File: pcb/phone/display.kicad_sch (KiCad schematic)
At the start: 6 parts

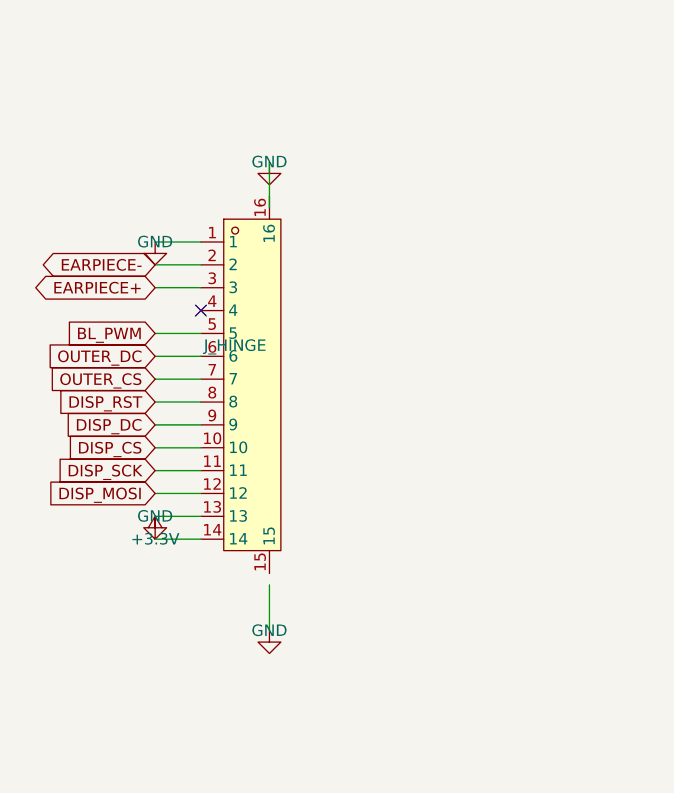
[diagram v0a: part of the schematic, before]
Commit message: Fix display sheet: J_HINGE mounting tab pins 15/16 GND connection
The J_HINGE connector (0.5K-HX-14PWB FPC) has 16 pins in its lib_symbol
definition: 14 signal pins + 2 mounting tabs (pins 15/16). The mounting
tabs need to be connected to GND.

Two issues fixed:
1. Removed phantom pin 15/16 definitions from the symbol instance that
   didn't match the 14-pin lib_symbol (but the lib_symbol itself does
   define 16 pins including the mounting tabs)
2. The GND wires for pins 15/16 were 1.27mm short of the actual pin
   connection points. Extended wire endpoints from (133.81, 109.68) to
   (133.81, 108.41) and from (133.81, 151.59) to (133.81, 150.32) to
   reach the actual pin positions.

Result: Display sheet is now ERC-clean (0 errors, 0 warnings).
Total ERC violations dropped from 287 to 283.

Generated with [Devin](https://devin.ai)

Co-Authored-By: Devin <158243242+devin-ai-integration[bot]@users.noreply.github.com>
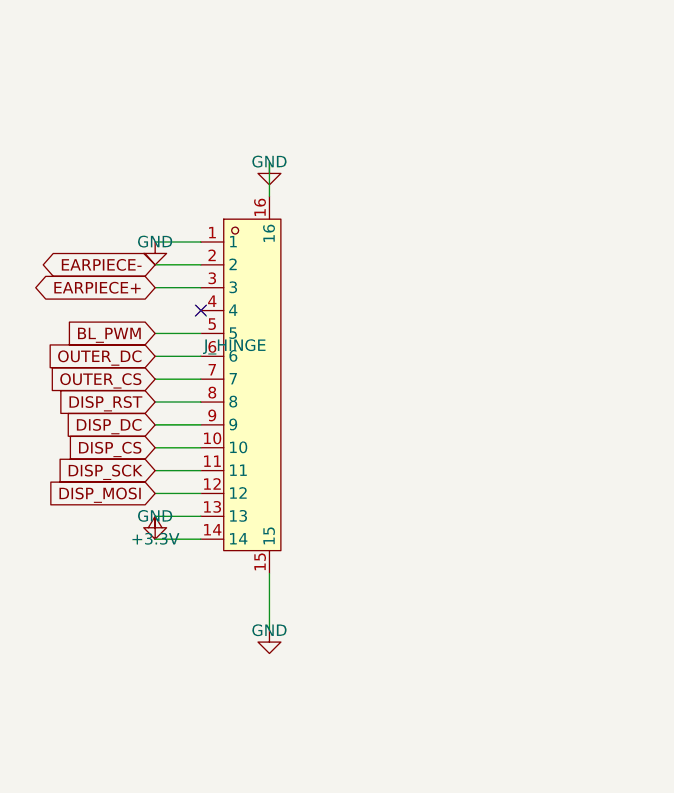
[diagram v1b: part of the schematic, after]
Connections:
- net GND: now also J_HINGE.15, J_HINGE.16
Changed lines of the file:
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@@
 		(wire
 			(pts
-				(xy 133.81 109.68) (xy 133.81 104.60)
-			)
-			(stroke
-				(width 0)
-				(type default)
-			)
-		)
-		(wire
-			(pts
-				(xy 133.81 151.59) (xy 133.81 156.67)
+				(xy 133.81 108.41) (xy 133.81 104.60)
+			)
+			(stroke
+				(width 0)
+				(type default)
+			)
+		)
+		(wire
+			(pts
+				(xy 133.81 150.32) (xy 133.81 156.67)
 			)
 			(stroke
@@
 			(pin "13")
 			(pin "14")
-			(pin "15")
-			(pin "16")
 			(instances (project "phone" (path "/451c3b43-1616-42cb-bf96-d436f4db82c2/d7f57b90-9db7-4266-b1f1-7949b1054009" (reference "J_HINGE") (unit 1))))
 		)

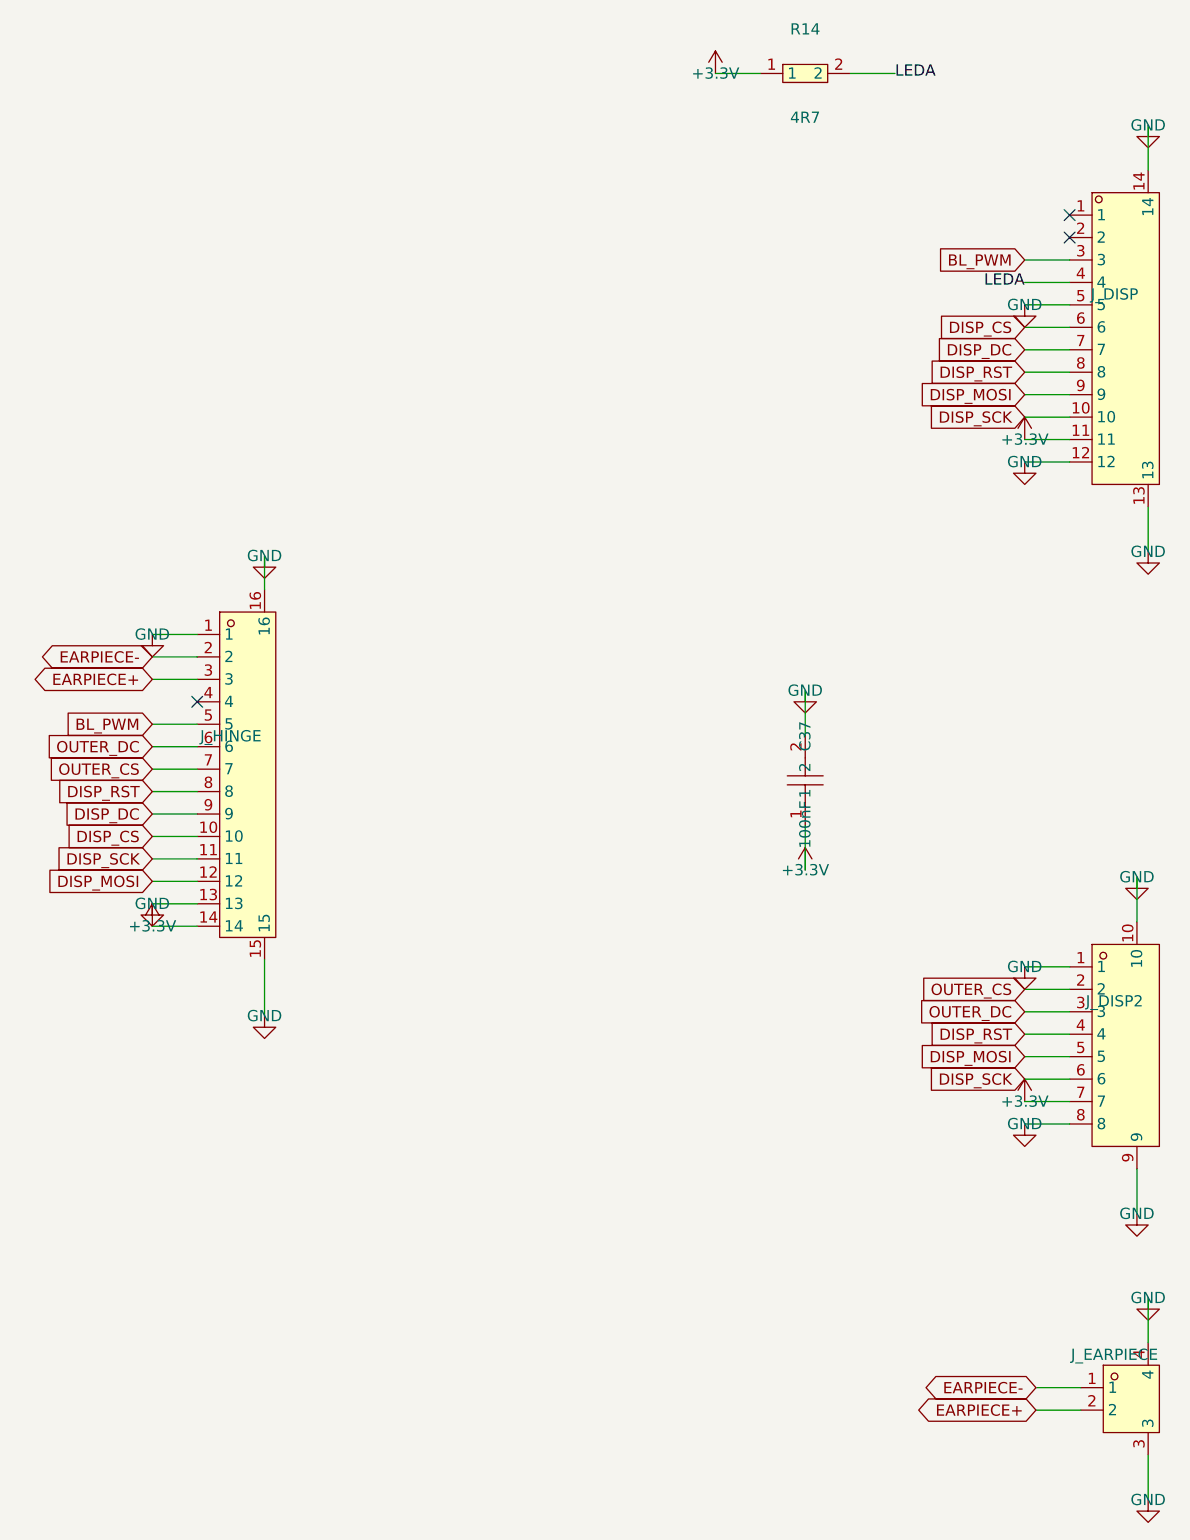
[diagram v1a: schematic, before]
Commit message: Split display sheet into main board + daughterboard
The flip/clamshell design has two PCBs connected via hinge flex. The display
sheet previously contained all display connectors on one sheet, which didn't
match the physical architecture.

Changes:
- display.kicad_sch: Now contains ONLY J_HINGE (hinge flex connector) and
  its associated wires, labels, and power symbols. Title updated to
  "Display (Main Board)".
- display_daughter.kicad_sch (new): Contains J_DISP (main display panel),
  J_DISP2 (outer display panel), J_EARPIECE (earpiece speaker), R14
  (backlight resistor), C37 (decoupling cap), and their associated wires,
  labels, and power symbols. Title: "Display Daughterboard".
- phone.kicad_sch: Added hierarchical sheet instance for Display_Daughter
  at (254, 340), page 6.

Global labels (DISP_MOSI, DISP_SCK, DISP_CS, DISP_DC, DISP_RST, OUTER_CS,
OUTER_DC, BL_PWM, EARPIECE+, EARPIECE-, +3.3V, GND) continue to connect
correctly across sheets via global label connectivity.

ERC result: 274 violations (all pre-existing on root sheet). Display and
Display_Daughter sheets are both ERC-clean.

Generated with [Devin](https://devin.ai)

Co-Authored-By: Devin <158243242+devin-ai-integration[bot]@users.noreply.github.com>
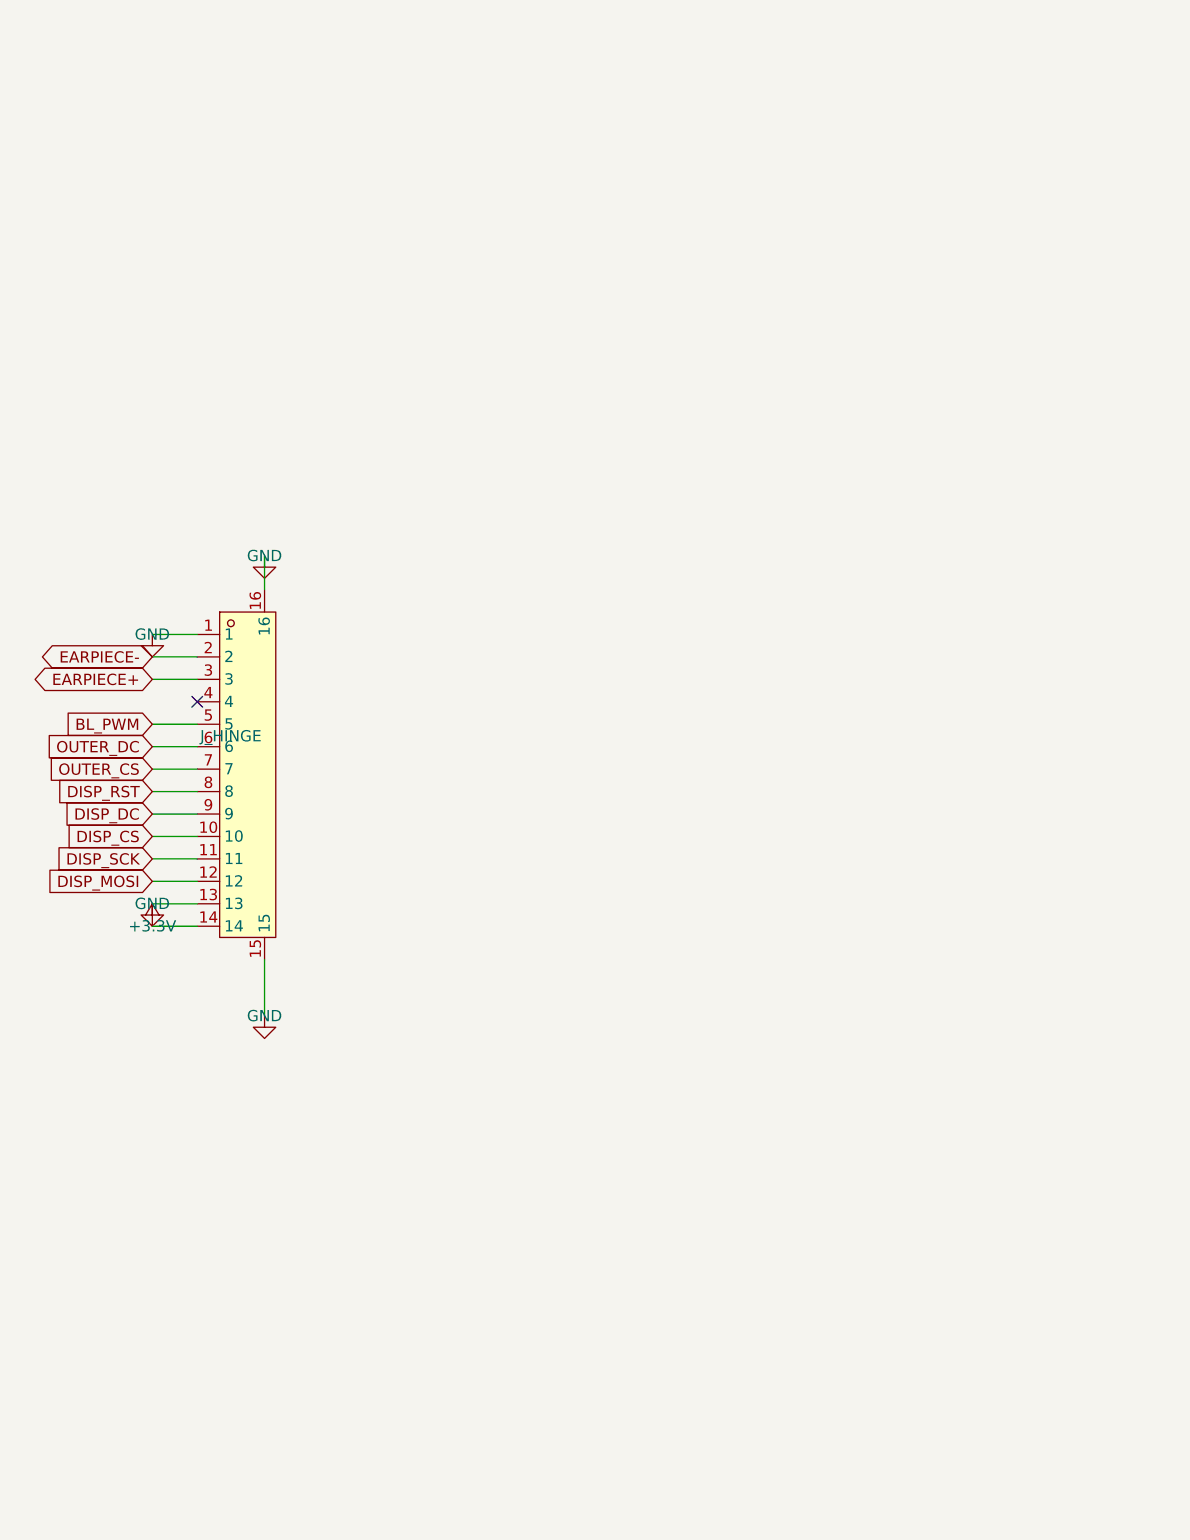
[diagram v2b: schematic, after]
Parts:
- removed C37: 100nF, easyeda2kicad:C0603, symbol passives:CC0603KRX7R9BB104
- removed J_DISP: 0.5K-HX-12PWB, easyeda2kicad:FPC-SMD_12P-P0.50_HDGC_0.5K-HX-12PWB, symbol connectors:0.5K-HX-12PWB
- removed J_DISP2: 0.5K-HX-8PWB, easyeda2kicad:FPC-SMD_8P-P0.50_HDGC_0.5K-HX-8PWB, symbol connectors:0.5K-HX-8PWB
- removed J_EARPIECE: S2B-PH-SM4-TB, easyeda2kicad:CONN-SMD_P2.00_S2B-PH-SM4-TB-LF-SN, symbol connectors:S2B-PH-SM4-TB
- removed R14: 4R7, easyeda2kicad:R0603, symbol passives:RC0603JR-07470RL
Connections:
- no-connect marks 3 -> 1
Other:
- title: Display -> Display (Main Board)

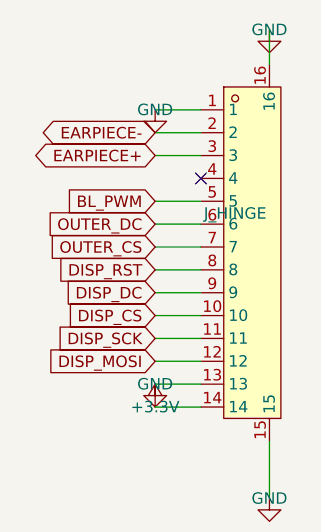
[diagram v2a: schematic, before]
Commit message: User edits: keypad rewiring, sheet reorder, ERC severity reverts, R24 fix
Keypad (keypad.kicad_sch):
- Rotated all 20 switches 270 degrees for vertical contact orientation
- Wired all 4 pins on each switch (pins 1&2 to column, pins 3&4 to row)
- Removed all 37 no_connect markers on pins 3&4
- Cleaned up to 25.4mm (1-inch) grid spacing
- Added pull-down resistors to all 4 columns (was only KEY_COL3)

Root sheet (phone.kicad_sch):
- Reordered sub-sheet blocks (Display_Daughter before SIM_SD)
- Cleaned up PWR_FLAG symbol formatting/indentation
- Reordered PWR_FLAG and +BATT symbol placement

MCU sheet (mcu.kicad_sch):
- Repositioned +3.3V power symbol (#PWR32) at pin 190.5,200.66

Project settings (phone.kicad_pro):
- Reverted ERC suppressions: endpoint_off_grid, isolated_pin_label,
  lib_symbol_mismatch back to warning (want actual fixes, not ignores)
- Added SW2-20 to used designators
- Reordered sheets list (Display_Daughter before SIM_SD)

Other sheets (codec, display, display_daughter, sim_sd):
- KiCad editor reformatting upon save

Generated with [Devin](https://devin.ai)

Co-Authored-By: Devin <158243242+devin-ai-integration[bot]@users.noreply.github.com>
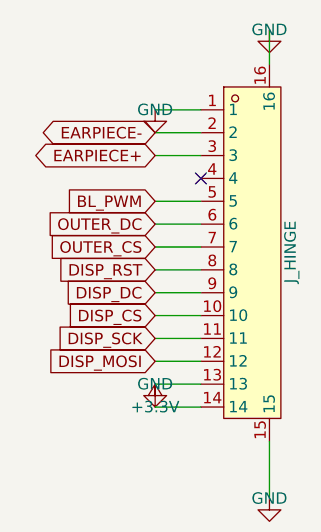
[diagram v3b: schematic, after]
